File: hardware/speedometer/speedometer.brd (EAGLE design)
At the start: 108.9 x 50.2 mm, 139 parts, among them IC1 PIC32MX110F016B-I_SO, IC10 24LC024SN, IC11 MAX16054AZT+T, IC12 TPS63001DRCT, IC13 TPS63002DRCT, IC2 CSTCE8M00G55-R0, IC3 CSTCE12M0G15L99-R0, IC4 MCP2200-I_SO, IC6 PCF8574T, IC7 BQ24075RGTT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

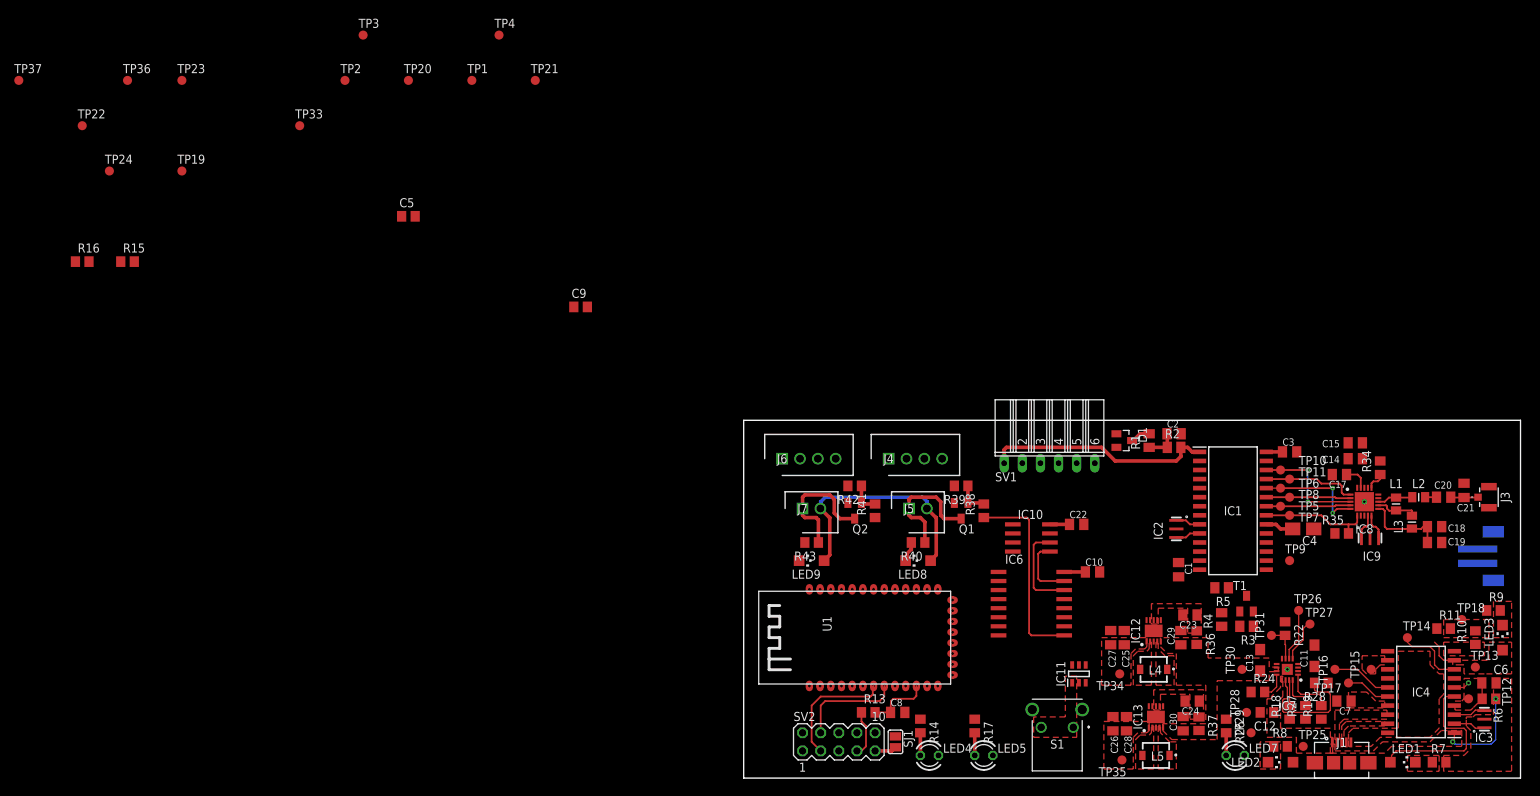
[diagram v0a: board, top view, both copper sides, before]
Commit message: Most of the work is done. Fixing ground planes and power paths
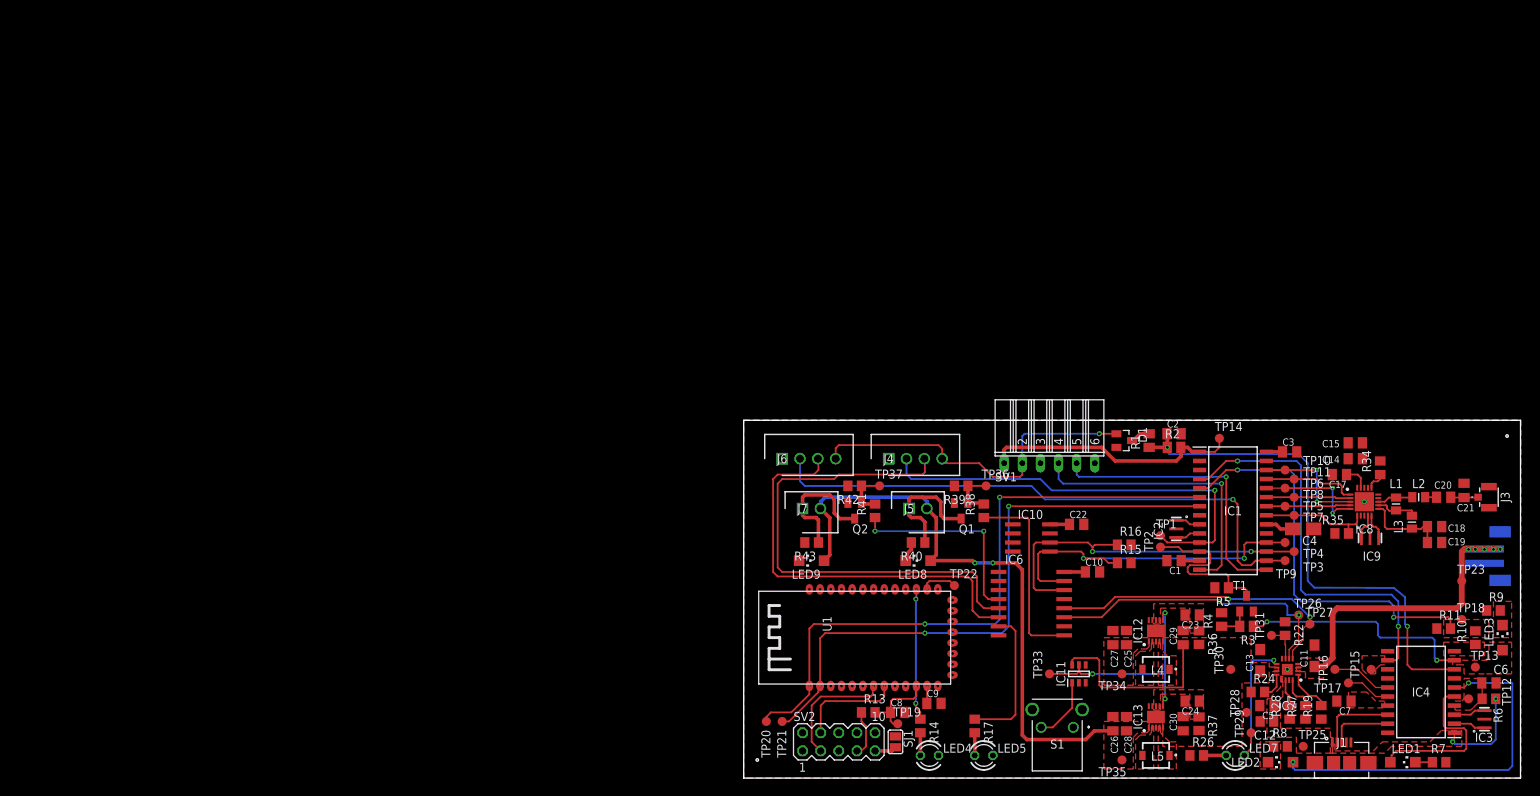
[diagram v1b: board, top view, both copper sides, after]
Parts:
- removed R18: 100, rcl:R0805
- removed TP24: TPB1,27, testpad:B1,27
- C5, C9: device rcl:C0805 -> rcl:C0805K
- moved TP23 192.6 mm to (100.6, 27.6)
- moved R16 151.3 mm to (53.3, 32.7)
- moved TP3 149.2 mm to (77.2, 31.8)
- moved R15 145.9 mm to (53.3, 30.2)
- moved C5 138.5 mm to (73.3, 10.2), turned to 180 degrees
- moved TP22 138.2 mm to (29.5, 27.0)
- moved TP37 133.4 mm to (19.1, 41.0)
- moved TP36 133.1 mm to (34.0, 41.0)
- moved TP2 131.7 mm to (58.4, 32.4), turned to 90 degrees
- moved TP4 131.1 mm to (75.9, 33.0)
- moved TP33 130.2 mm to (42.9, 14.6), turned to 90 degrees
- moved TP19 126.8 mm to (21.6, 7.62)
- moved TP1 115.7 mm to (58.4, 34.0)
- moved TP20 102.9 mm to (3.17, 7.94)
- moved TP21 96.3 mm to (5.40, 7.94)
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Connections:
- removed net N$11: IC7.15, R18.2, TP24.TP
- removed net N$16: IC6.4, R17.1
- new net N$3: IC6.7, R17.1
- net !MCLR: no longer TP14.TP
- net !SYSOFF: no longer R18.1
- net GND: now also IC7.15
- net LASER_LEFT_CTL: now also IC6.4; no longer IC6.7
- net LEFT_STS: now also IC6.6; no longer IC6.5
- net N$42: now also TP14.TP
- net RIGHT_STS: now also IC6.5; no longer IC6.6
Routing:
- net BT_U1RX: track 0.00 -> 89.6 mm, vias 0 -> 2
- net BT_U1TX: track 0.00 -> 85.1 mm, vias 0 -> 2
- net INT_LEFT: track 0.00 -> 80.9 mm, vias 0 -> 1
- net RIGHT_STS: track 0.00 -> 70.4 mm
- net INT_RIGHT: track 0.00 -> 61.5 mm, vias 0 -> 1
- net !MCLR: track 14.4 -> 72.9 mm, vias 0 -> 2
- net LEFT_STS: track 0.00 -> 58.2 mm
- net DBG_U2RX: track 0.00 -> 57.0 mm, vias 0 -> 2
- net DBG_U2TX: track 0.00 -> 56.9 mm, vias 0 -> 2
- net +3V3: track 7.99 -> 62.3 mm, vias 0 -> 1
- net +5V: track 33.8 -> 83.8 mm, vias 0 -> 2
- net N$50: track 2.26 -> 51.9 mm, vias 1 -> 2
- net N$10: track 0.00 -> 40.9 mm, vias 0 -> 5
- net SDA: track 9.05 -> 49.8 mm, vias 0 -> 2
- net PGEC3: track 0.00 -> 40.4 mm, vias 0 -> 1
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- added copper zone on layer 16, net GND
- added copper zone on layer 1, net N$10
- removed copper zone on layer 1, net N$51
- removed copper zone on layer 1, net N$58
- removed copper zone on layer 1, net USB_D+
- removed copper zone on layer 1, net USB_D-

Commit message: Routing is done. Waiting a check from a Sandro
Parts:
- C1, C10, C2, C22, C23, C24, C3, C6, C7, C8, C9: device rcl:C0805K -> rcl:C0603K
- C12: device rcl:C0805 -> rcl:C0603K
- moved C7 1.71 mm to (85.7, 10.2)
- moved TP20 1.62 mm to (2.86, 9.53)
- moved TP21 1.59 mm to (5.40, 9.53)
- moved SV2 1.27 mm to (14.6, 5.08)
- moved SJ1 0.95 mm to (22.2, 5.08)
- moved R35 0.95 mm to (82.9, 34.3), turned to 270 degrees
- moved R26 0.64 mm to (64.1, 3.17)
- moved TP29 0.64 mm to (70.5, 6.35)
- moved C17 0.32 mm to (83.5, 42.9)
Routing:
- net +3V3: track 62.3 -> 306.5 mm, vias 1 -> 19
- net N$60: track 0.00 -> 11.5 mm
- net N$62: track 0.00 -> 11.1 mm
- net +5V: track 83.8 -> 88.5 mm, vias 2 -> 4
- net N$4: track 0.00 -> 3.66 mm
- net N$52: track 0.00 -> 3.06 mm
- net N$20: track 0.00 -> 2.87 mm
- net !BAT_CHG: track 21.1 -> 23.2 mm
- net N$10: track 40.9 -> 42.1 mm
- net DBG_DATA: track 14.7 -> 13.6 mm
- net N$49: track 24.2 -> 23.3 mm
- net IRQ: track 15.6 -> 14.8 mm
- net DBG_CLK: track 17.3 -> 16.6 mm
- net BT_U1TX: track 85.1 -> 84.5 mm
- net N$53: track 9.08 -> 8.44 mm
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- added copper zone on layer 16, net N$10
- removed copper zone on layer 1, net N$4
- removed copper zone on layer 1, net N$52
- removed copper zone on layer 1, net N$60
- removed copper zone on layer 1, net N$62

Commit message: WIP
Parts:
- removed SV1: (no value), con-lsta:FE06W
- added ICSP: (no value), con-lsta:FE06W
- T1: value (none) -> BC817-16LT1SMD; device transistor-neu-to92:SOT23-BEC -> transistor-npn:SOT23-BEC
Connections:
- net +3V3: now also ICSP.2; no longer SV1.2
- net GND: now also ICSP.3; no longer SV1.3
- net N$42: now also ICSP.1; no longer SV1.1
- net PGEC3: now also ICSP.5; no longer SV1.5
- net PGED3: now also ICSP.4; no longer SV1.4
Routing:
- net N$42: track 36.3 -> 38.9 mm
- net PGED3: track 40.1 -> 42.0 mm
- net PGEC3: track 40.4 -> 42.3 mm
- net +3V3: track 306.5 -> 305.4 mm
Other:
- board text added: "BT"
- board text added: "PWR"
- board text added: "PWR_BTN"
- board text added: "Speed'o'Meter v1.0"
- board text added: "github.com/gabbla/speedometer"

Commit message: laser sensor gerber updated
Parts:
- added JMP1, JMP2, JMP3, JMP4: 0R-JUMPA, jump-0r-smd:A0R-JMP
- added Q3, Q4: BC817, transistor-npn:SOT23-BEC
- added R12, R20, R21, R25: 10k, rcl:R0805
- added R18, R23: 100k, rcl:R0805
- ICSP: device con-lsta:FE06W -> con-lsta:FE06
- moved TP31 3.51 mm to (74.3, 23.5)
- moved TP19 3.31 mm to (20.6, 10.8)
- moved C7 1.27 mm to (87.0, 10.2)
- moved TP33 1.27 mm to (41.6, 14.6)
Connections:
- new net N$11: J6.4, JMP4.2
- new net N$13: Q4.B, R21.2, R23.1
- new net N$16: J7.2, JMP2.2, LED9.A
- new net N$21: J4.4, JMP3.2
- new net N$26: Q3.B, R12.2, R18.1
- new net N$27: J4.2, R12.1
- new net N$28: J6.2, R21.1
- new net N$6: J5.2, JMP1.2, LED8.A
- net +3V3: now also JMP1.1, JMP2.1, JMP3.1, JMP4.1, R20.2, R25.2; no longer J4.4, J6.4
- net +5V: now also JMP1.3, JMP2.3, JMP3.3, JMP4.3; no longer J5.2, J7.2, LED8.A, LED9.A
- net GND: now also Q3.E, Q4.E, R18.2, R23.2
- net INT_LEFT: now also Q4.C, R25.1; no longer J6.2
- net INT_RIGHT: now also Q3.C, R20.1; no longer J4.2
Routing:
- net +3V3: track 305.4 -> 353.3 mm, vias 19 -> 23
- net +5V: track 88.5 -> 109.1 mm, vias 4 -> 6
- net INT_RIGHT: track 61.5 -> 76.3 mm, vias 1 -> 2
- net N$6: track 0.00 -> 10.1 mm
- net N$16: track 0.00 -> 10.1 mm
- net N$13: track 0.00 -> 9.64 mm
- net INT_LEFT: track 80.9 -> 90.5 mm, vias 1 -> 2
- net N$26: track 0.00 -> 4.62 mm
- net N$11: track 0.00 -> 3.57 mm
- net !BAT_PGOOD: track 5.20 -> 8.19 mm
- net N$28: track 0.00 -> 2.69 mm
- net N$27: track 0.00 -> 2.56 mm
- net N$21: track 0.00 -> 2.27 mm
- net N$1: track 11.3 -> 9.16 mm
- net N$4: track 3.66 -> 2.39 mm
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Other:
- board text added: "5V - 3V3"
- board text added: "CHG"
- board text added: "LEDs"
- board text added: "RX - TX"
- board text added: "Speed'o'Meter v0.1-alpha"
- board text removed: "Speed'o'Meter v1.0"

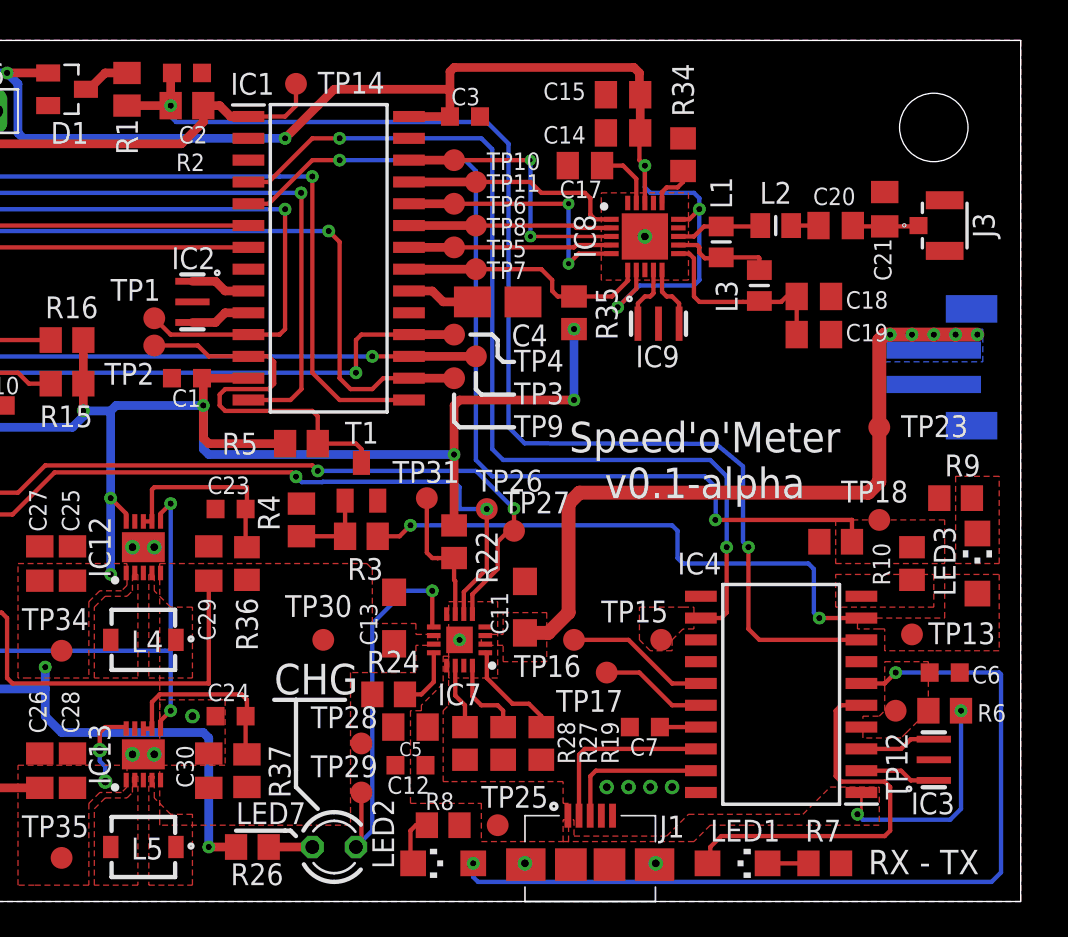
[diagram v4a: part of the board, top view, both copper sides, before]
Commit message: TPS6300x inductors changed
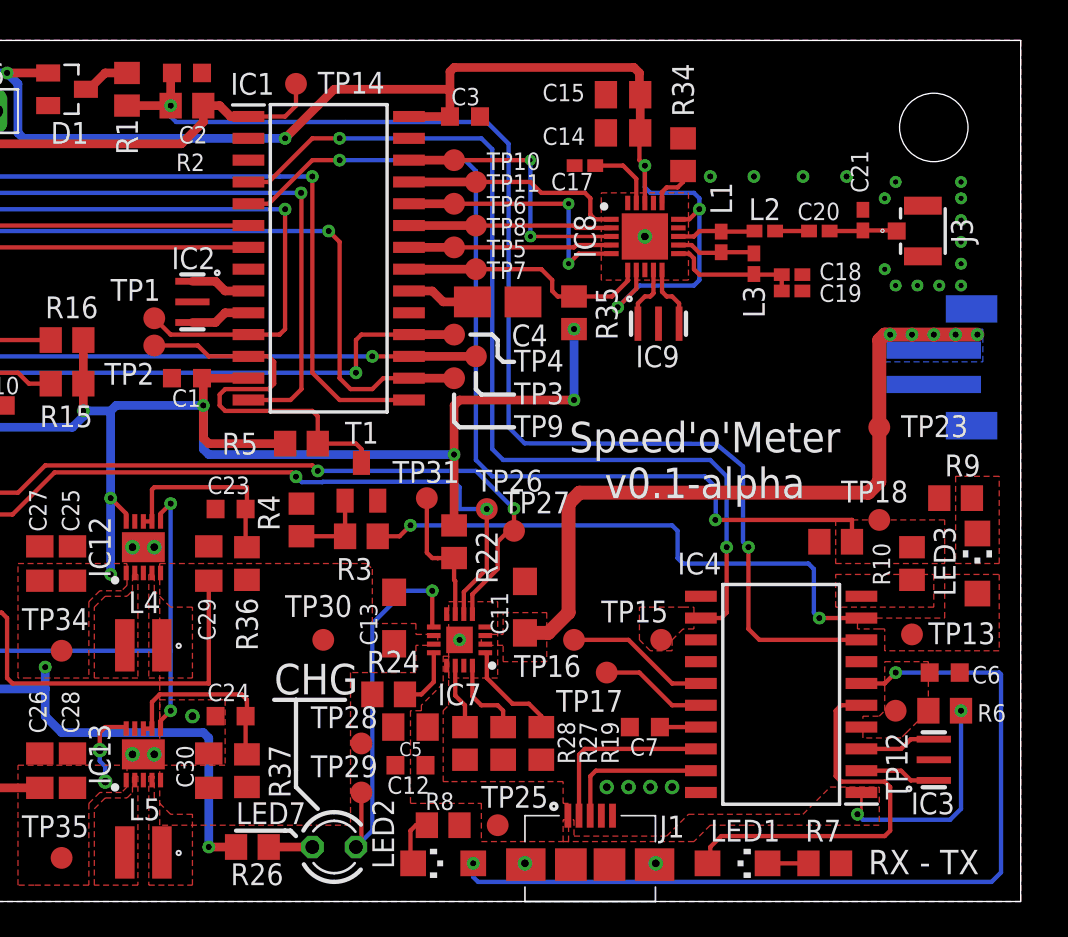
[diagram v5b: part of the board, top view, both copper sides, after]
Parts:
- C17, C18, C19, C20, C21: device rcl:C0805K -> rcl:C0402K
- L1, L2, L3: device LQM21PN2R2MC0D:INDC2012X55N -> 0402_inductor:C0402K
- L4, L5: device VLF4012AT-3R3M1R3:VLF4012A -> LPS3015-222MRB:LPS3015
- R1, R2, R3, R4, R5: device resistor:M0805 -> rcl:R0805
- R14: value 560 -> 620
- R37: device rcl:M0805 -> rcl:R0805
- moved C19 2.84 mm to (95.6, 35.6)
- moved C18 1.80 mm to (95.6, 36.5)
- moved C21 1.42 mm to (99.7, 39.7)
- moved L3 1.31 mm to (93.3, 37.1)
- moved J3 1.31 mm to (103.2, 39.1)
- moved C20 1.00 mm to (97.2, 39.1)
- moved L2 0.71 mm to (94.0, 39.1)
- moved L4 0.32 mm to (57.8, 14.9)
- moved L5 0.32 mm to (57.8, 2.86)
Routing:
- net N$35: track 11.8 -> 7.90 mm
- net N$33: track 5.95 -> 4.99 mm

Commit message: Main board gerber updated
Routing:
- net +5V: track 109.1 -> 108.3 mm, vias 6 -> 4
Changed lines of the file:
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@@
 <contactref element="L2" pad="1"/>
 <contactref element="L1" pad="1"/>
-<wire x1="93.0275" y1="39" x2="93.38" y2="39.0525" width="0.1524" layer="1"/>
 <wire x1="89.8525" y1="38.735" x2="88.945" y2="38.735" width="0.254" layer="1"/>
 <wire x1="91.44" y1="39.0175" x2="91.405" y2="39.0525" width="0.254" layer="1"/>
 <wire x1="90.17" y1="39.0525" x2="89.8525" y2="38.735" width="0.254" layer="1"/>
 <wire x1="91.405" y1="39.0525" x2="90.17" y2="39.0525" width="0.254" layer="1"/>
-<wire x1="91.44" y1="39.0175" x2="93.345" y2="39.0175" width="0.254" layer="1"/>
 <wire x1="93.345" y1="39.0175" x2="93.38" y2="39.0525" width="0.254" layer="1"/>
+<wire x1="93.38" y1="39.0525" x2="93.345" y2="39.0175" width="0.254" layer="1"/>
+<wire x1="93.345" y1="39.0175" x2="91.44" y2="39.0175" width="0.254" layer="1"/>
 </signal>
 <signal name="N$33">
@@
 <contactref element="L3" pad="1"/>
 <contactref element="IC8" pad="12"/>
-<wire x1="91.44" y1="37.8175" x2="91.3875" y2="37.465" width="0.1524" layer="1"/>
 <wire x1="91.44" y1="37.8175" x2="91.405" y2="37.7825" width="0.254" layer="1"/>
 <wire x1="90.17" y1="37.7825" x2="91.405" y2="37.7825" width="0.254" layer="1"/>
 <wire x1="88.945" y1="38.235" x2="89.7175" y2="38.235" width="0.254" layer="1"/>
 <wire x1="89.7175" y1="38.235" x2="90.17" y2="37.7825" width="0.254" layer="1"/>
-<wire x1="91.44" y1="37.8175" x2="93.275" y2="37.8175" width="0.254" layer="1"/>
-<wire x1="93.275" y1="37.8175" x2="93.345" y2="37.7475" width="0.254" layer="1"/>
+<wire x1="91.44" y1="37.8175" x2="91.475" y2="37.7825" width="0.254" layer="1"/>
+<wire x1="93.345" y1="37.7475" x2="93.275" y2="37.8175" width="0.254" layer="1"/>
+<wire x1="93.275" y1="37.8175" x2="91.44" y2="37.8175" width="0.254" layer="1"/>
 </signal>
 <signal name="N$35">
@@
 <wire x1="56.6975" y1="10.16" x2="55.5625" y2="10.16" width="0.254" layer="1"/>
 <wire x1="55.5625" y1="10.16" x2="55.245" y2="9.8425" width="0.254" layer="1"/>
-<via x="55.245" y="8.8174" extent="1-16" drill="0.45"/>
-<wire x1="55.245" y1="8.1824" x2="55.5625" y2="7.8649" width="0.254" layer="16"/>
-<wire x1="55.5625" y1="7.8649" x2="55.5625" y2="6.985" width="0.254" layer="16"/>
-<via x="55.5625" y="6.985" extent="1-16" drill="0.45"/>
-<wire x1="55.245" y1="9.8425" x2="55.245" y2="8.8174" width="0.254" layer="1"/>
 <contactref element="JMP1" pad="3"/>
 <contactref element="JMP2" pad="3"/>
@@
 <wire x1="27.305" y1="42.8625" x2="27.383546875" y2="42.941046875" width="0.4064" layer="16"/>
 <via x="27.383546875" y="42.941046875" extent="1-16" drill="0.35"/>
-<wire x1="55.245" y1="8.8174" x2="55.245" y2="8.1824" width="0.254" layer="16"/>
+<wire x1="55.245" y1="9.8425" x2="55.245" y2="7.62" width="0.254" layer="1"/>
 </signal>
 <signal name="N$38">

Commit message: Fixed some stuff with Sandro's help. Main board gerber updated
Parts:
- moved TP1 1.91 mm to (56.5, 34.0)
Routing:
- net N$50: track 51.9 -> 36.9 mm
- net +5V: track 108.3 -> 110.3 mm
- net +3V3: track 353.3 -> 355.2 mm
- net INT_RIGHT: track 76.3 -> 78.2 mm
- net GND: track 0.00 -> 0.22 mm, vias 29 -> 69

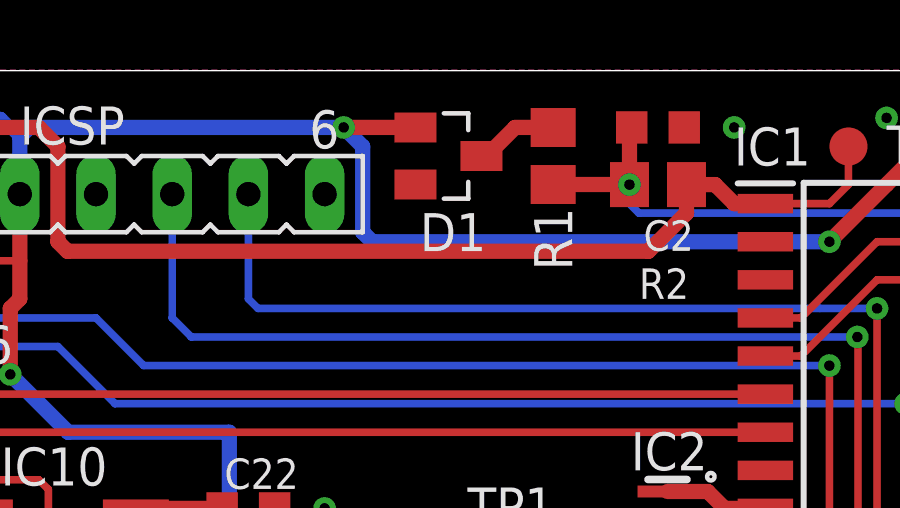
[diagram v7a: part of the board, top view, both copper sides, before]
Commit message: Fixed diode (#8) and battery polarity (#5)
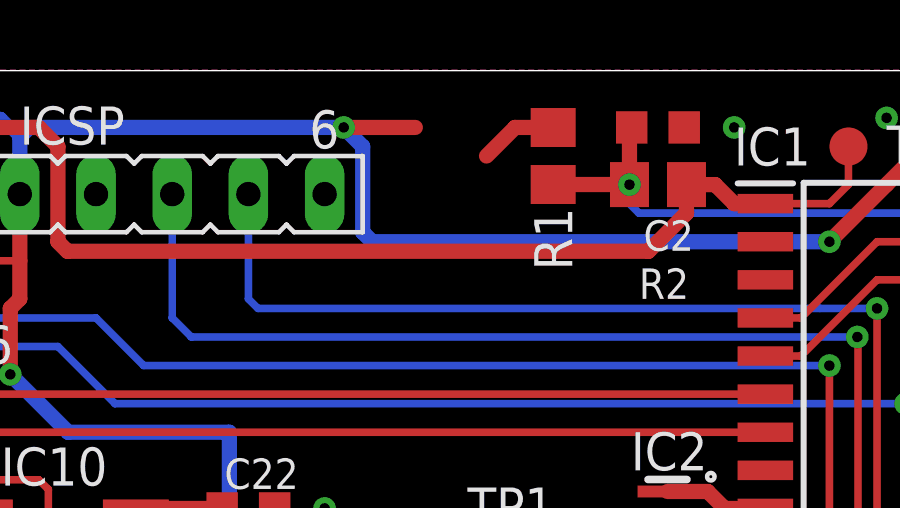
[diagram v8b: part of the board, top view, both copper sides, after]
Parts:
- removed D1: BAT54, diode:SOT23
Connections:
- removed net N$45: D1.3, R1.2
- net +3V3: now also R1.2; no longer D1.1
- net GND: now also J2.1; no longer J2.2
- net N$10: now also J2.2; no longer J2.1
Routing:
- net N$45: track 2.79 -> 0.00 mm
- net +3V3: track 355.2 -> 357.9 mm
